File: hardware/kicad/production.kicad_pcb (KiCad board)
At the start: 2 copper layers, 143.3 x 107 mm, 41 parts

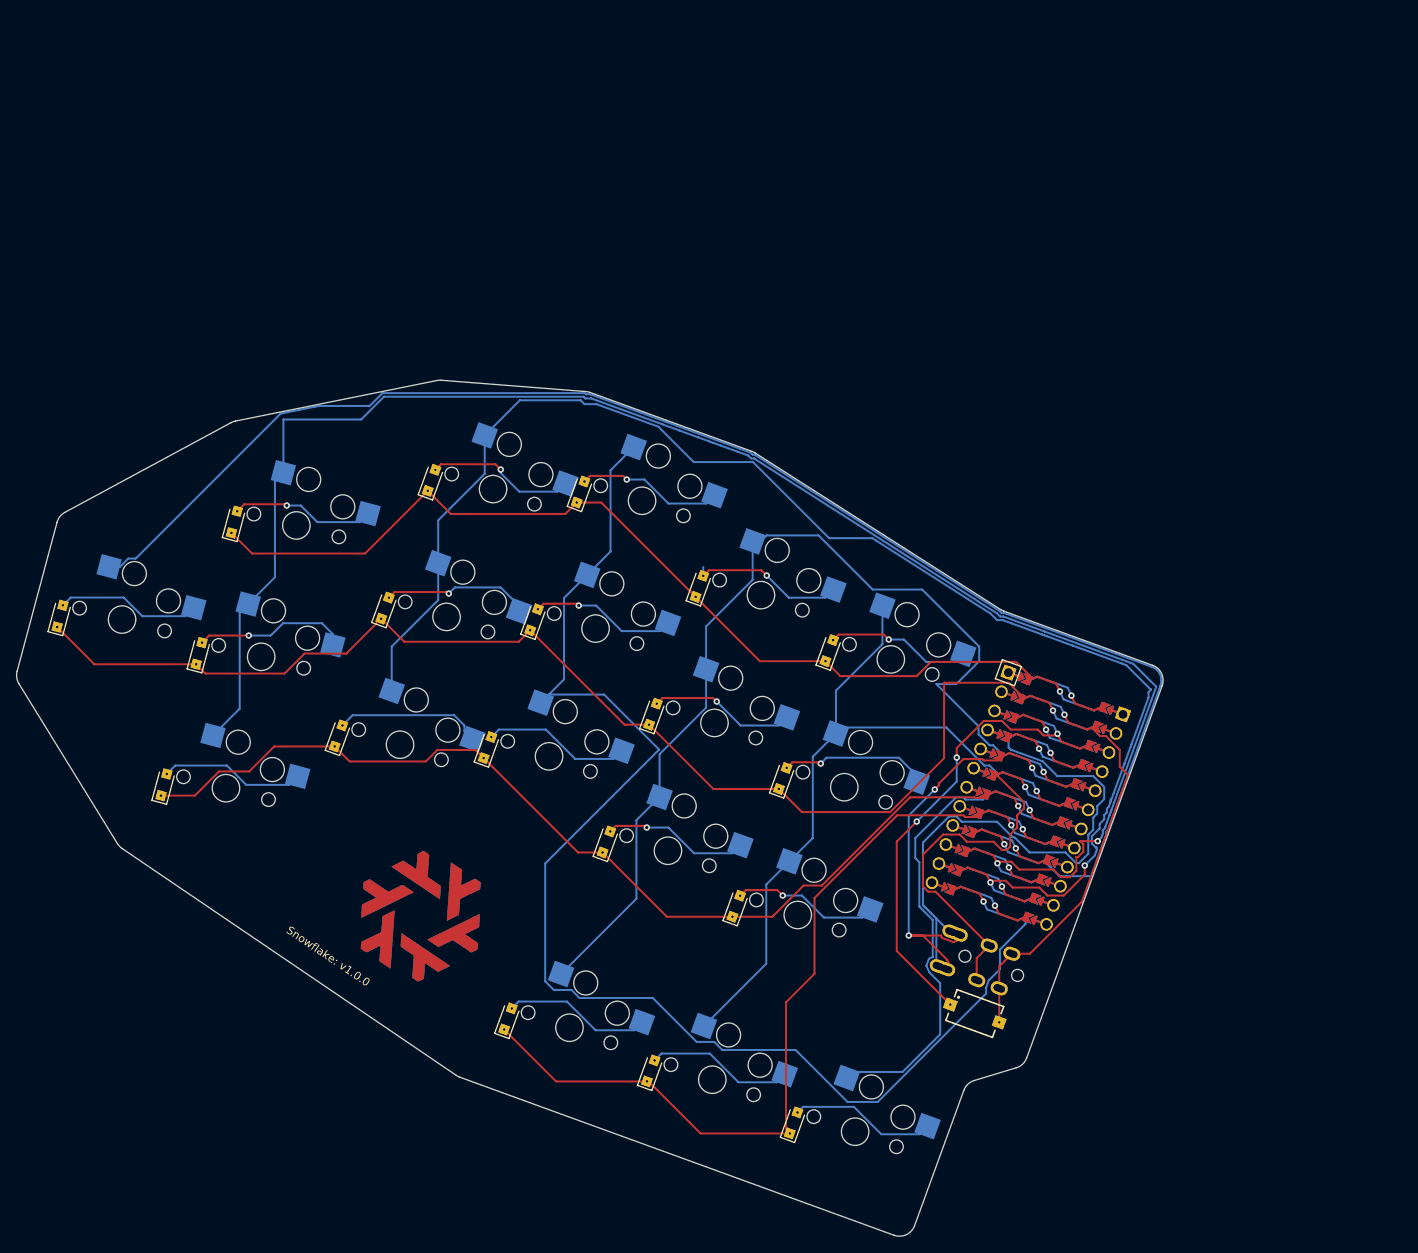
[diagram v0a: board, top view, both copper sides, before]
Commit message: Fixed main issue with v.1.0.0: Made switches reversable
- Added 'nix run .#watch-pcb' command.
- made switches reverseable
- rewired
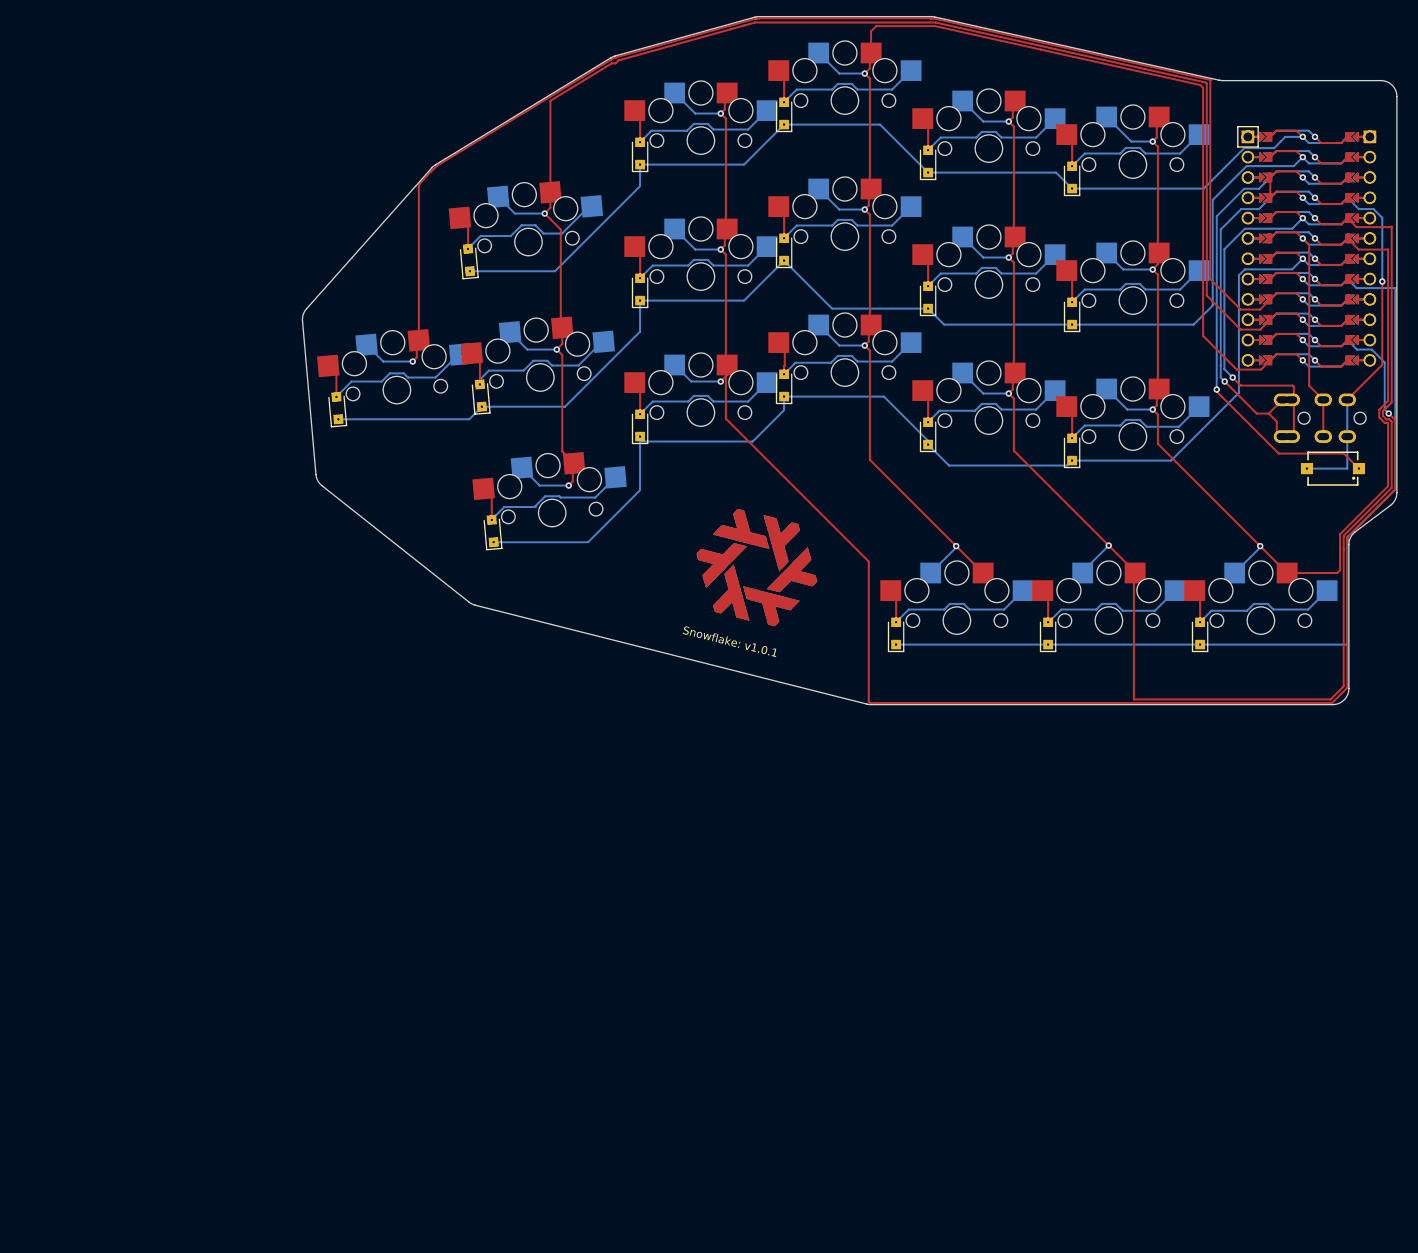
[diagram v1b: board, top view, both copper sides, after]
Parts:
- moved TRRS1 82.6 mm to (220.5, 88.9), turned to -90 degrees
- moved S19 81.6 mm to (206.5, 111.9), turned to 0 degrees
- moved S20 81.5 mm to (215.5, 92.9), turned to 180 degrees
- moved D19 79.5 mm to (198.9, 113.5), turned to 90 degrees
- moved MCU1 77.2 mm to (212.5, 65.4), turned to -90 degrees
- moved S18 75.8 mm to (187.5, 111.9), turned to 0 degrees
- moved D18 73.9 mm to (179.9, 113.5), turned to 90 degrees
- moved S14 73.0 mm to (190.5, 88.9), turned to 0 degrees
- moved D14 70.9 mm to (182.9, 90.5), turned to 90 degrees
- moved S15 70.7 mm to (190.5, 71.9), turned to 0 degrees
- moved S17 70.3 mm to (168.5, 111.9), turned to 0 degrees
- moved S16 68.9 mm to (190.5, 54.9), turned to 0 degrees
- moved D15 68.5 mm to (182.9, 73.5), turned to 90 degrees
- moved D17 68.4 mm to (160.9, 113.5), turned to 90 degrees
- moved S11 67.1 mm to (172.5, 86.9), turned to 0 degrees
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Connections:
- S17 pad 1: P21 -> P9
- S18 pad 1: P20 -> P21
- S19 pad 1: P19 -> P20
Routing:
- net P21: track 130.4 -> 213.6 mm, vias 1 -> 5
- net P20: track 95.7 -> 158.8 mm, vias 1 -> 5
- net P19: track 62.8 -> 10.9 mm
- net P8: track 184.3 -> 228.8 mm, vias 2 -> 5
- net VCC: track 80.9 -> 50.9 mm, vias 1 -> 2
- net P3: track 55.4 -> 36.8 mm
- net P9: track 179.2 -> 195.9 mm, vias 1 -> 5
- net P4: track 133.2 -> 147.9 mm
- net P6: track 193.4 -> 180.0 mm, vias 1 -> 2
- net P5: track 108.4 -> 121.0 mm
- net P7: track 212.3 -> 203.6 mm, vias 2 -> 4
- net matrix_pinky_top: track 18.1 -> 22.8 mm, vias 1 -> 0
- net matrix_outer_home: track 18.2 -> 22.4 mm
- net matrix_middle_bottom: track 18.6 -> 22.8 mm
- net matrix_inner_bottom: track 18.4 -> 22.5 mm, vias 1 -> 0
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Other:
- board size 143.3 x 107 mm -> 136.8 x 86 mm
- board text added: "Snowflake: v1.0.1"
- board text removed: "Snowflake: v1.0.0"

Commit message: Applied nix formatter.
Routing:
- net P21: track 213.6 -> 211.0 mm
- net P8: track 228.8 -> 227.5 mm

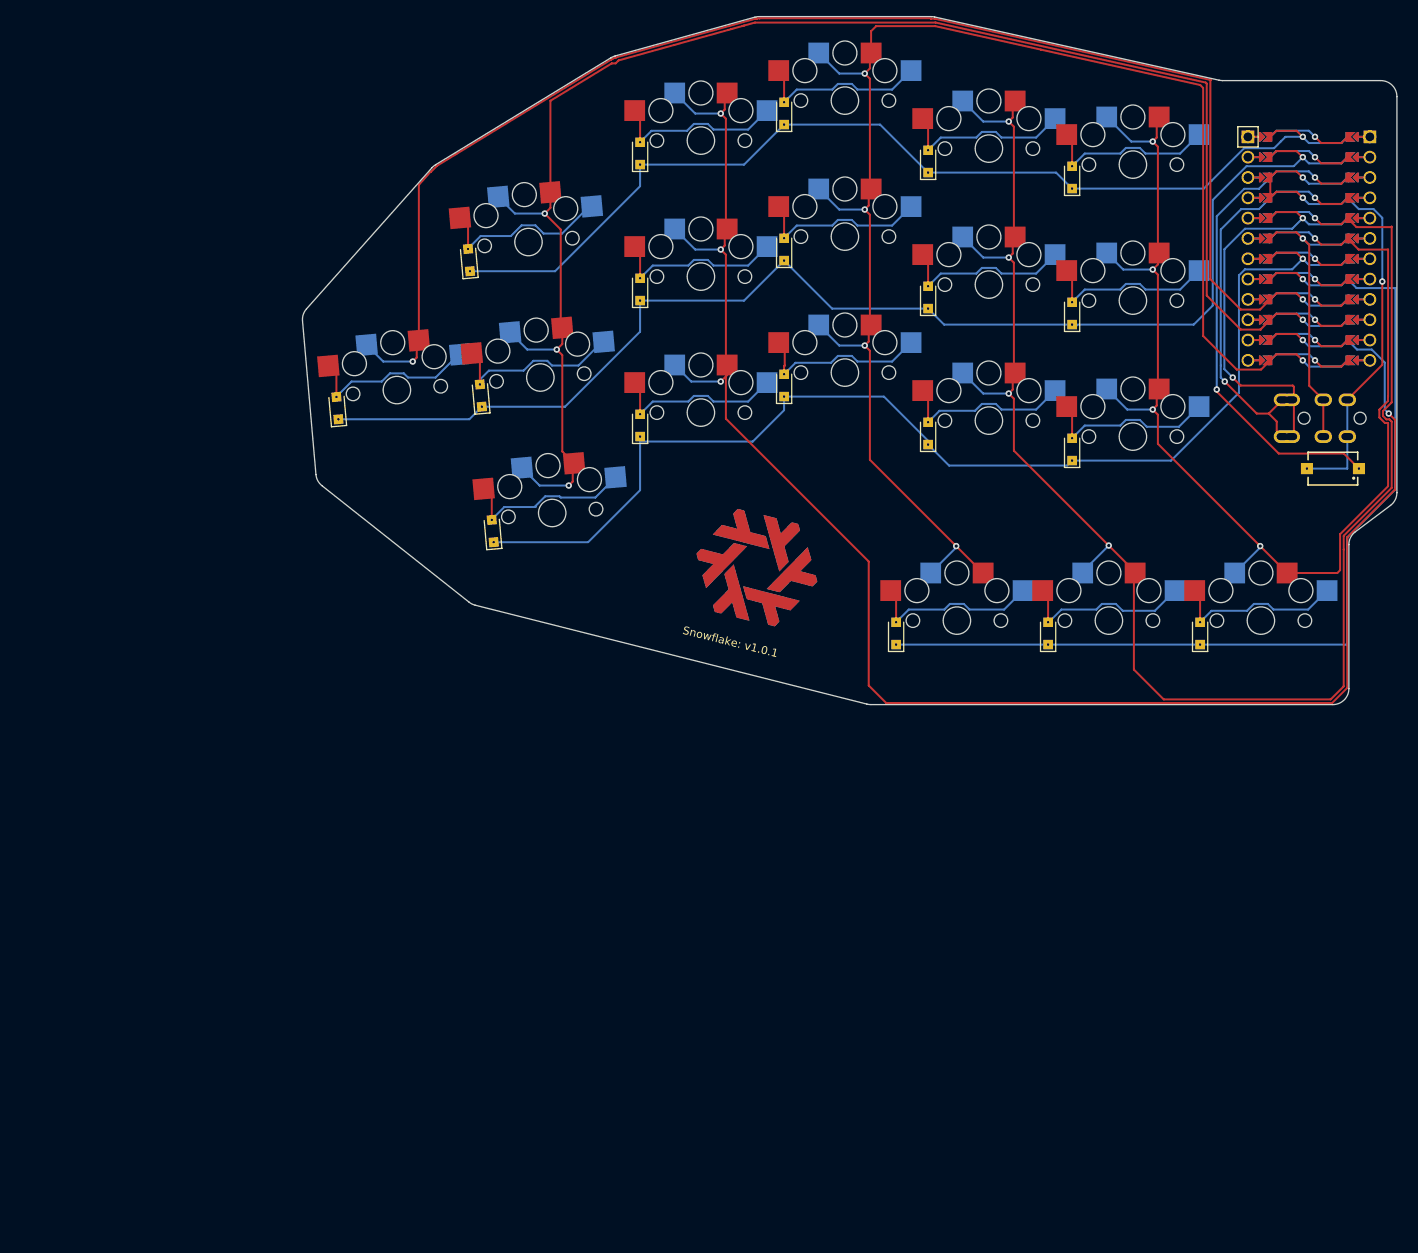
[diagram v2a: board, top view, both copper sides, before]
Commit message: Added mounting holes.
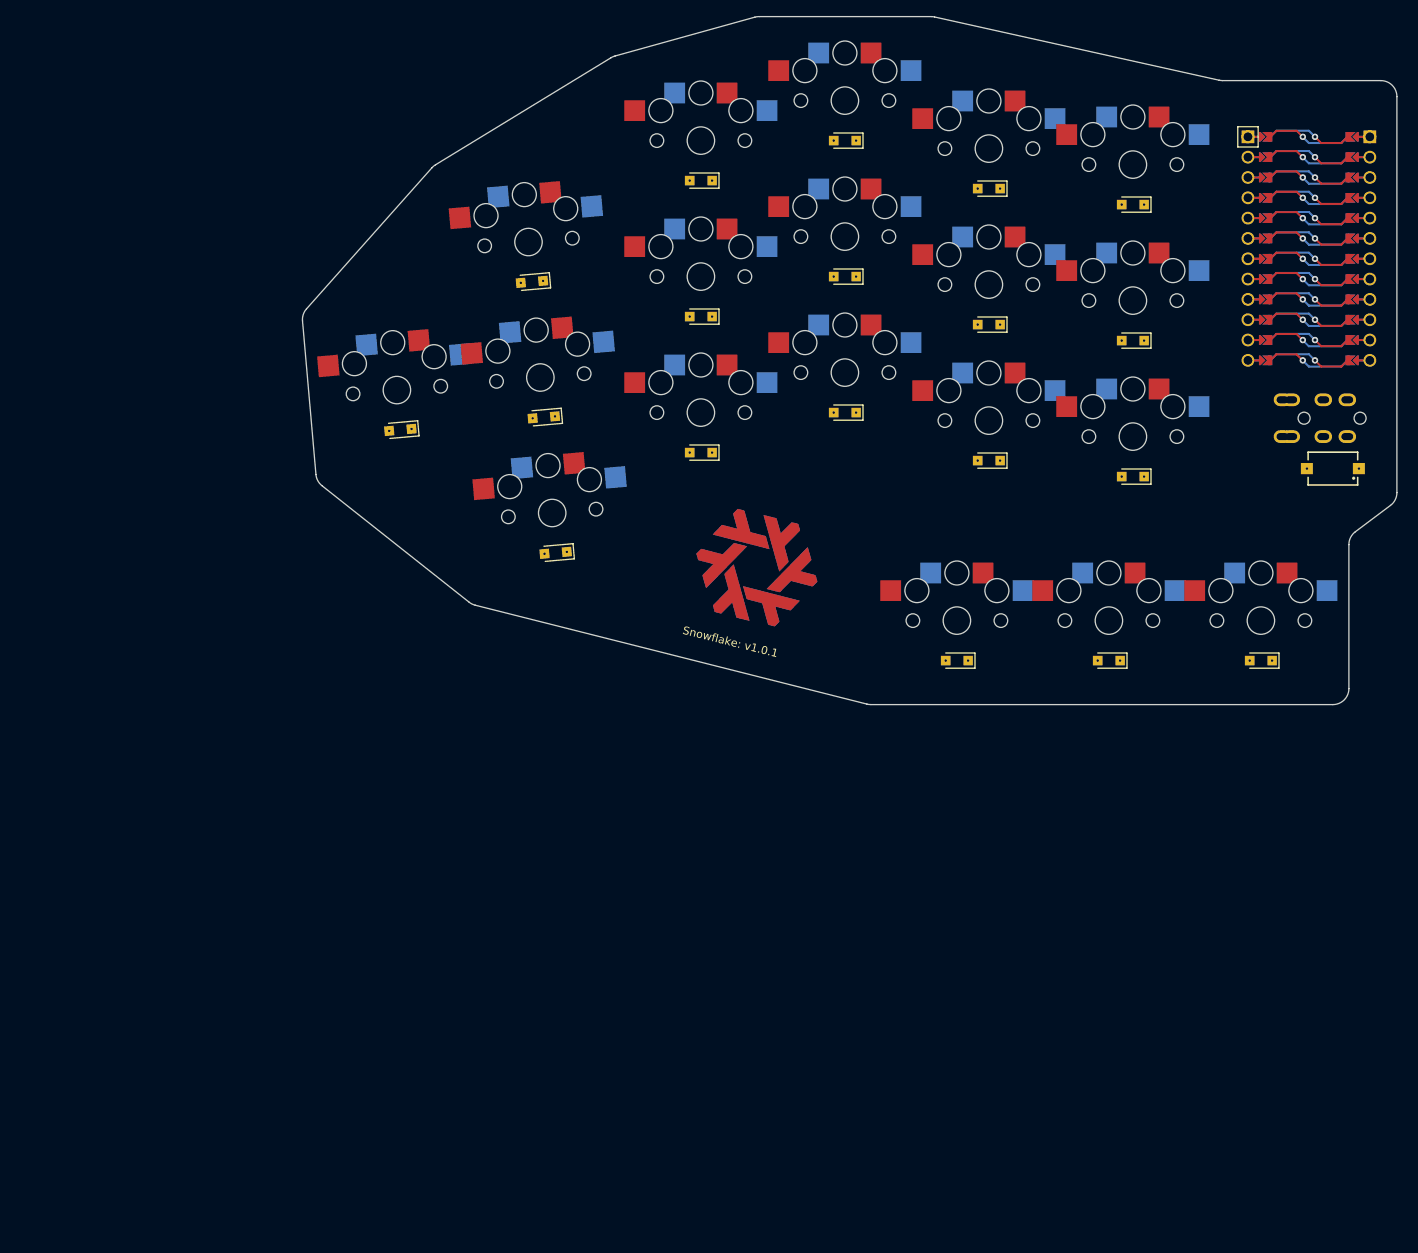
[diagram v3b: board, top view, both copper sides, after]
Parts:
- D1, D10, D11, D12, D13, D14, D15, D16, D17, D18, D19, D2, D3, D4, D5, D6, D7, D8, D9: moved to 
- moved D11 8.33 mm to (172.5, 91.9), turned to 180 degrees
- moved D12 8.33 mm to (172.5, 74.9), turned to 180 degrees
- moved D8 8.33 mm to (154.5, 85.9), turned to 180 degrees
- moved D9 8.33 mm to (154.5, 68.9), turned to 180 degrees
- moved D10 8.33 mm to (154.5, 51.9), turned to 180 degrees
- moved D13 8.33 mm to (172.5, 57.9), turned to 180 degrees
- moved D2 8.33 mm to (118.4, 103.4), turned to 185 degrees
- moved D1 8.33 mm to (99.0, 88.0), turned to 185 degrees
- moved D14 8.33 mm to (190.5, 93.9), turned to 180 degrees
- moved D15 8.33 mm to (190.5, 76.9), turned to 180 degrees
- moved D17 8.33 mm to (168.5, 116.9), turned to 180 degrees
- moved D18 8.33 mm to (187.5, 116.9), turned to 180 degrees
- moved D19 8.33 mm to (206.5, 116.9), turned to 180 degrees
- moved D5 8.33 mm to (136.5, 90.9), turned to 180 degrees
- moved D6 8.33 mm to (136.5, 73.9), turned to 180 degrees
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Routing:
- net (no net): track 0.00 -> 262.1 mm
- net P8: track 227.5 -> 0.00 mm, vias 5 -> 1
- net P21: track 211.0 -> 0.00 mm, vias 5 -> 1
- net P7: track 203.6 -> 0.00 mm, vias 4 -> 1
- net P9: track 195.9 -> 0.00 mm, vias 5 -> 1
- net P6: track 180.0 -> 0.00 mm, vias 2 -> 1
- net P0: track 162.3 -> 0.00 mm
- net P20: track 158.8 -> 0.00 mm, vias 5 -> 1
- net P4: track 147.9 -> 0.00 mm
- net P1: track 130.2 -> 0.00 mm
- net P5: track 121.0 -> 0.00 mm
- net GND: track 78.9 -> 0.00 mm, vias 4 -> 3
- net RST: track 63.3 -> 0.00 mm, vias 2 -> 1
- net P2: track 53.2 -> 0.00 mm, vias 2 -> 1
- net VCC: track 50.9 -> 0.00 mm, vias 2 -> 1
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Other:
- net class Default added: clearance 0.2, trace_width 0.25, via_dia 0.8, via_drill 0.4
